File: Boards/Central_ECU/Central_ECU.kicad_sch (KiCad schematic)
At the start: 18 parts, among them U1 STM32G0B1RCTx

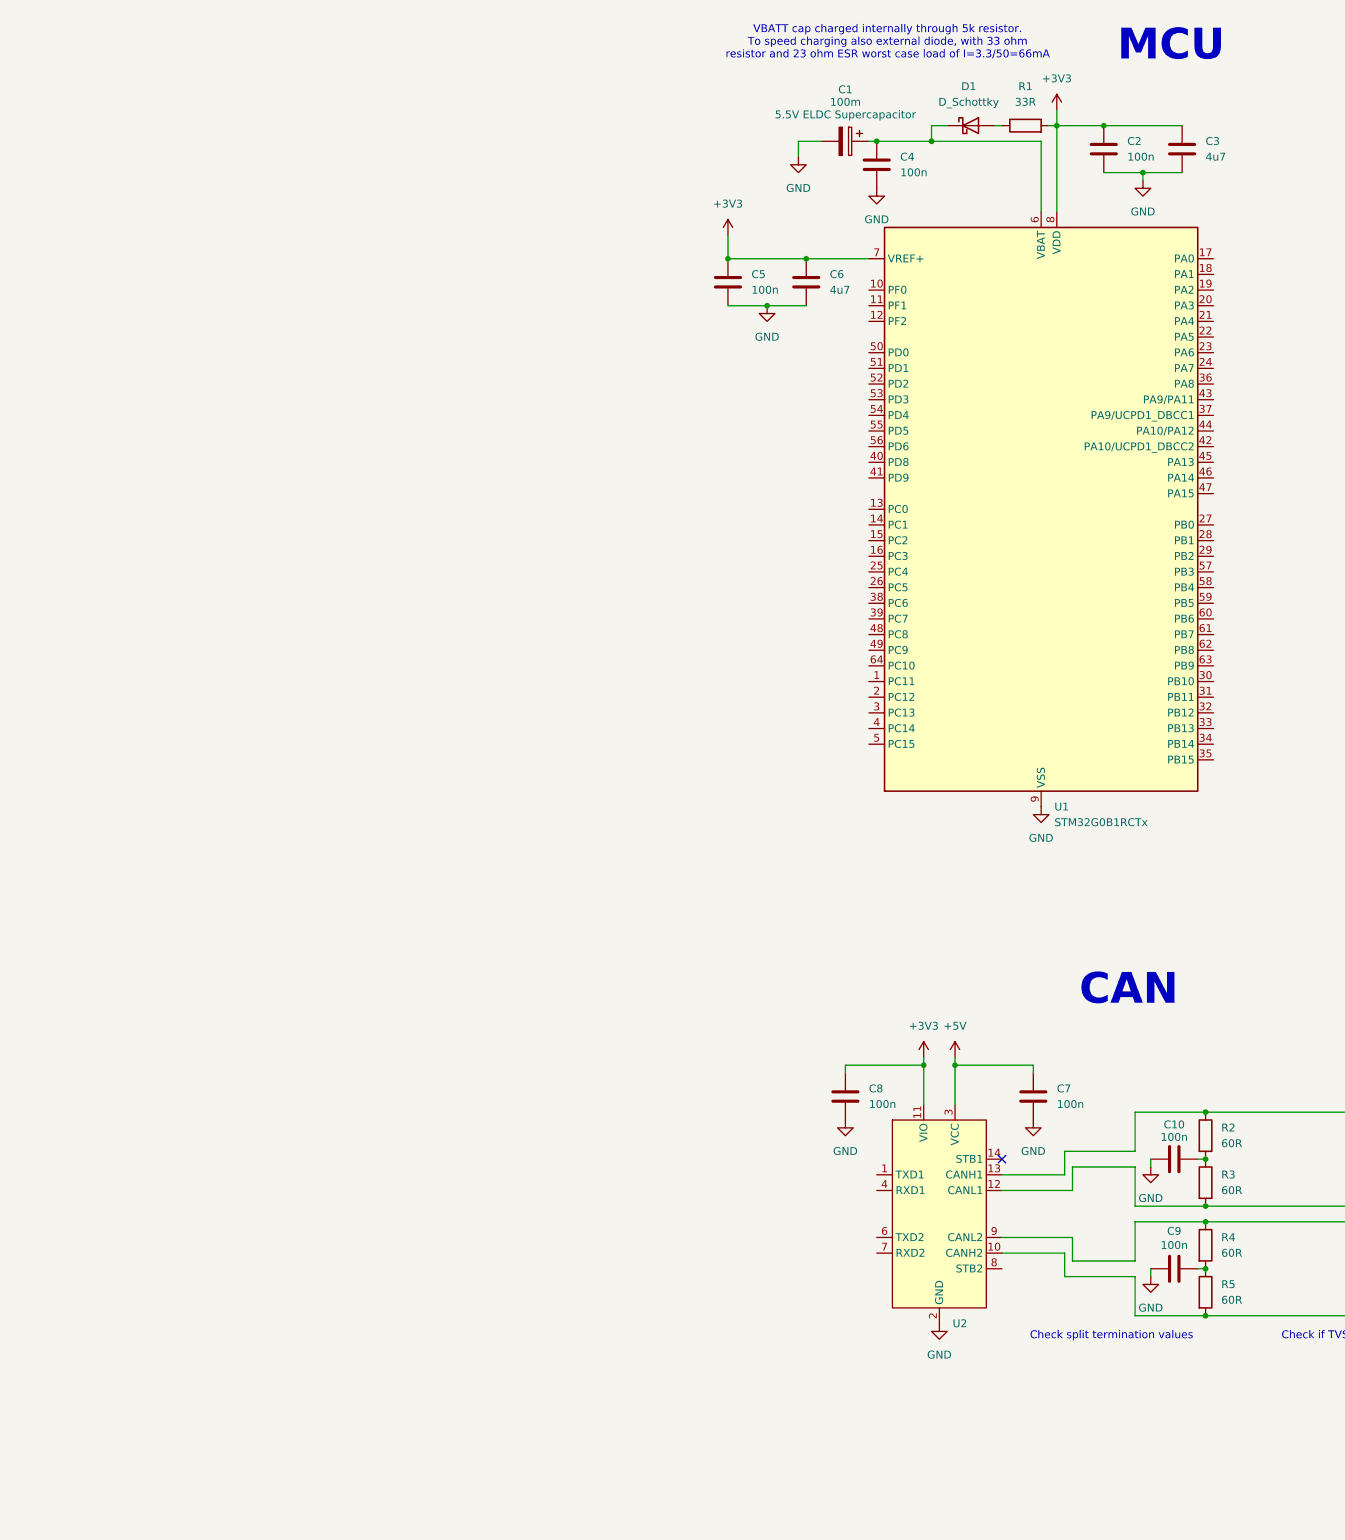
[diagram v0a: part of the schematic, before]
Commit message: Added 422 and crystal
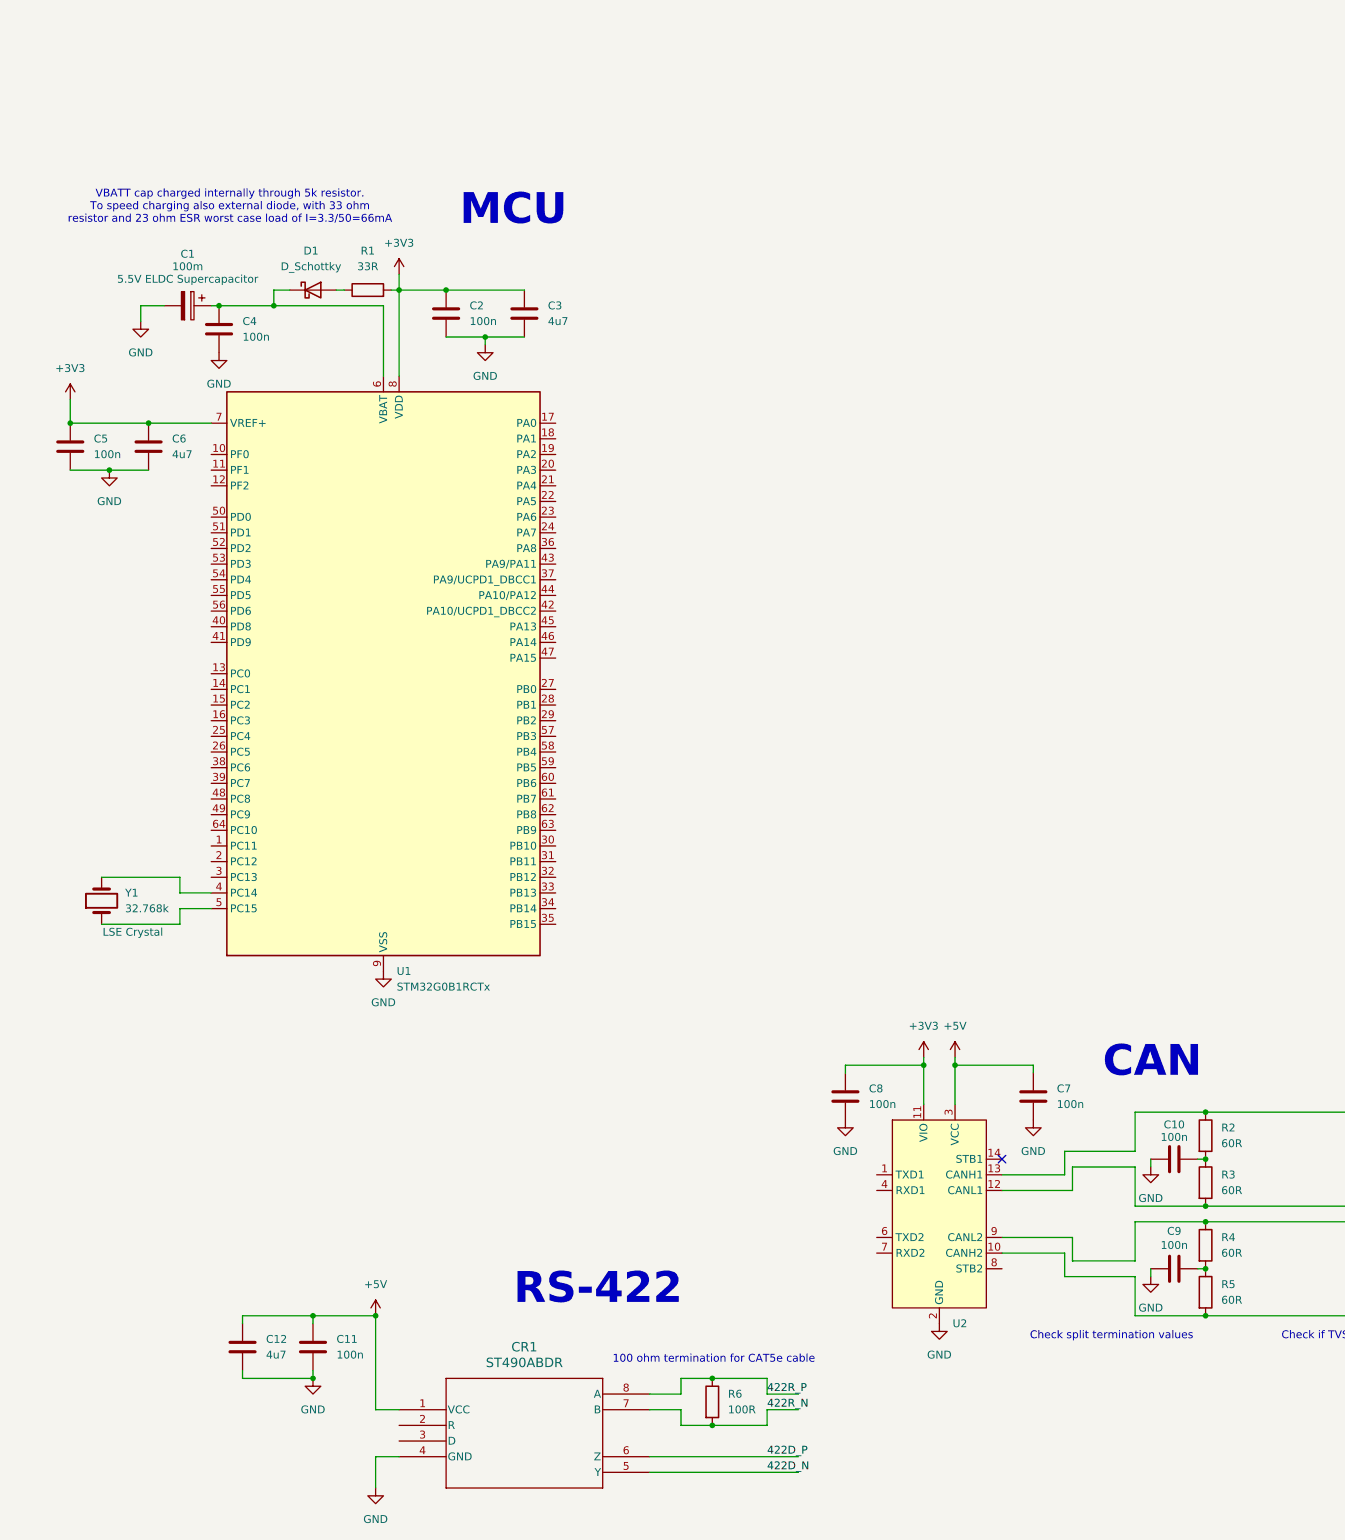
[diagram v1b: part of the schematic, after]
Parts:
- added C11: 100n, symbol Device:C
- added C12: 4u7, symbol Device:C
- added CR1: ST490ABDR, Package_SO:SO-8_3.9x4.9mm_P1.27mm, symbol TS_Symbols:ST490ABDR
- added R6: 100R, symbol Device:R
- added Y1: 32.768k, Crystal:Crystal_SMD_2012-2Pin_2.0x1.2mm, symbol Device:Crystal
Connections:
- net +5V: now also C11.1, C12.1, CR1.1 (VCC)
- net GND: now also C11.2, C12.2, CR1.4 (GND)
- net at U1.4 (PC14): now also Y1.2
- net at U1.5 (PC15): now also Y1.1
- new net 422D_N: CR1.5 (Y)
- new net 422D_P: CR1.6 (Z)
- new net 422R_N: CR1.7 (B), R6.2
- new net 422R_P: CR1.8 (A), R6.1
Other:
- note added: "100 ohm termination for CAT5e cable"
- note added: "RS-422"
- moved on the sheet: C1, C2, C3, C4, C5, C6, D1, R1, U1

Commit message: More to the central mcu plus started on ignitors and valve control
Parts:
- added C13, C14: 12p, symbol Device:C
- added C15, C16: C, symbol Device:C
- added Y2: 8MHz, symbol Device:Crystal
- U1: MPN (none) -> STM32G0B1RCT6
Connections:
- net GND: now also C13.2, C14.2, C15.2, C16.2
- net USART1_RX: now reaches CR1.2 (R)
- net USART1_RX: now also U1.61 (PB7)
- net USART1_TX: now reaches CR1.3 (D)
- net USART1_TX: now also U1.60 (PB6)
- net CAN2_RX: now reaches U2.1 (TXD1)
- net CAN2_RX: now also U1.27 (PB0)
- net CAN2_TX: now reaches U2.4 (RXD1)
- net CAN2_TX: now also U1.28 (PB1)
- net CAN1_RX: now reaches U2.6 (TXD2)
- net CAN1_RX: now also U1.25 (PC4)
- net CAN1_TX: now reaches U2.7 (RXD2)
- net CAN1_TX: now also U1.26 (PC5)
- net at U1.10 (PF0): now also C15.1, Y2.1
- net at U1.11 (PF1): now also C16.1, Y2.2
- net I2C3_SCL: now reaches U1.13 (PC0)
- net I2C3_SDA: now reaches U1.14 (PC1)
- net ADC_0: now reaches U1.17 (PA0)
- net ADC_1: now reaches U1.18 (PA1)
- net ADC_2: now reaches U1.19 (PA2)
- net ADC_3: now reaches U1.20 (PA3)
- net ADC_4: now reaches U1.21 (PA4)
- net SPI_SCK: now reaches U1.22 (PA5)
- net SPI_MISO: now reaches U1.23 (PA6)
- net SPI_MOSI: now reaches U1.24 (PA7)
- net at U1.4 (PC14), Y1.2: now also C14.1
- net USB_D-: now reaches U1.43 (PA9/PA11)
- net USB_D+: now reaches U1.44 (PA10/PA12)
- net SWDIO: now reaches U1.45 (PA13)
- net SWCLK: now reaches U1.46 (PA14)
- net at U1.5 (PC15), Y1.1: now also C13.1
- net UART2_TX: now reaches U1.55 (PD5)
- net UART2_RX: now reaches U1.56 (PD6)
- net I2C2_SCL: now reaches U1.57 (PB3)
- net I2C2_SDA: now reaches U1.58 (PB4)
- net I2C1_SCL: now reaches U1.62 (PB8)
- net I2C1_SDA: now reaches U1.63 (PB9)
- no-connect marks 1 -> 3
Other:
- added sheet Interlocked (ign+nc_valve.kicad_sch)
- moved on the sheet: C1, C10, C11, C12, C2, C3, C4, C5, C6, C7, C8, C9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

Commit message: Some more minor tweaks
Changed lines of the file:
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@@
 	)
 	(sheet
-		(at 437.515 117.475)
+		(at 313.055 194.945)
 		(size 85.09 51.435)
 		(exclude_from_sim no)
@@
 		)
 		(property "Sheetname" "Interlocked"
-			(at 437.515 116.7634 0)
+			(at 313.055 194.2334 0)
 			(effects
 				(font
@@
 		)
 		(property "Sheetfile" "ign+nc_valve.kicad_sch"
-			(at 437.515 169.4946 0)
+			(at 313.055 246.9646 0)
 			(effects
 				(font

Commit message: Added most connectors and hooking up
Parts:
- added J11: Micro_SD_Card, symbol Connector:Micro_SD_Card
- added R19, R20: 27R, symbol Device:R
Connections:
- net USB_D+: now also R20.2; no longer U1.44 (PA10/PA12)
- net USB_D-: now also R19.2; no longer U1.43 (PA9/PA11)
- net CANL2: now reaches R5.2, U2.10 (CANH2)
- net CANL1: now reaches R3.2, U2.12 (CANL1)
- net CANH1: now reaches R2.1, U2.13 (CANH1)
- net CANH2: now reaches R4.1, U2.9 (CANL2)
- net OX_LOW_SENSE: now reaches U1.1 (PC11)
- net EMATCH_1_CONT: now reaches U1.2 (PC12)
- net EMATCH_2_CONT: now reaches U1.3 (PC13)
- net CAN1_AUX: now reaches U1.32 (PB12)
- net CAN2_AUX: now reaches U1.33 (PB13)
- net PGOOD_HS: now reaches U1.34 (PB14)
- net IMON_HS: now reaches U1.35 (PB15)
- net ARM_HS: now reaches U1.38 (PC6)
- net EMATCH_1_FIRE: now reaches U1.39 (PC7)
- net EMATCH_2_FIRE: now reaches U1.48 (PC8)
- net OX_FIRE: now reaches U1.49 (PC9)
- net 12V_SENSE: now reaches U1.64 (PC10)
- net ADC_0 renamed ADC_0 (4S)
- net ADC_1 renamed ADC_1 (2S)
- new net: R19.1, U1.43 (PA9/PA11)
- new net: R20.1, U1.44 (PA10/PA12)
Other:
- added sheet Connectors (connectors.kicad_sch)
- sheet Interlocked ports: added 12V_SENSE, 4S_ARMED_V+, ARM_HS, EMATCH_1+, EMATCH_1-, EMATCH_1_CONT, EMATCH_1_FIRE, EMATCH_2+, EMATCH_2-, EMATCH_2_CONT, EMATCH_2_FIRE, IMON_HS, OX_FIRE, OX_LOW_SENSE, OX_SOLENOID_+, OX_SOLENOID_-, PGOOD_HS, VDDIO; removed none
- note added: "Micro SD"
- moved on the sheet: C1, C10, C11, C12, C13, C14, C15, C16, C2, C3, C4, C5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

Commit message: Nearing completion
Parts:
- added C38, C40: 10u, symbol Device:C
- added C39, C41: 100n, symbol Device:C
- added R35, R36, R37, R38: 20K, symbol Device:R
- added U8: SSD1306, Custom:SSD1306-0.91-OLED-4pin-128x32, symbol TS_Symbols:SSD1306_128x32
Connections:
- net +3V3: now also J11.4 (VDD), C38.1, C39.1, C40.1, C41.1, R35.1, R36.1, R37.1, R38.1, U8.2 (3V3)
- net GND: now also J11.6 (VSS), J11.9 (SHIELD), C38.2, C39.2, C40.2, C41.2, U8.1 (GND)
- net I2C3_SCL: now also U8.3 (SCL)
- net I2C3_SDA: now also U8.4 (SDA)
- net SPI_MISO: now also J11.7 (DAT0), R36.2
- net SPI_MOSI: now also J11.3 (CMD), R37.2
- net SPI_SCK: now also J11.5 (CLK), R35.2
- net SPI_SD_CS: now reaches U1.36 (PA8)
- net SPI_SD_CS: now also J11.2 (DAT3/CD), R38.2
- no-connect marks 3 -> 15
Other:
- sheet Connectors ports: added I2CA_SCL, I2CA_SDA, I2CB_SCL, I2CB_SDA, UART_RX, UART_TX; removed none
- note added: "Display"
- note added: "TODO: Add some LED's - Both power supplies - GPIO controlled Add a buzzer? Break out generic pins"
- moved on the sheet: C5, C6

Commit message: For review
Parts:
- added D2, D3, D4: LED, LED_SMD:LED_1206_3216Metric, symbol Device:LED
- added H1, H2, H3, H4: ~, MountingHole:MountingHole_3.2mm_M3_DIN965_Pad_TopOnly, symbol Mechanical:MountingHole_Pad
- added R13: 330R, Resistor_SMD:R_0805_2012Metric, symbol Device:R
- added R14: 220R, Resistor_SMD:R_0805_2012Metric, symbol Device:R
- added R15: 1K, Resistor_SMD:R_0805_2012Metric, symbol Device:R
- added R16, R17, R18, R19: 10K, Resistor_SMD:R_0805_2012Metric, symbol Device:R
- added TP1: RTC_CAP, TestPoint:TestPoint_Keystone_5005-5009_Compact, symbol Connector:TestPoint_Small
- added TP10: CANTX2, TestPoint:TestPoint_Keystone_5005-5009_Compact, symbol Connector:TestPoint_Small
- added TP11: CANRX2, TestPoint:TestPoint_Keystone_5005-5009_Compact, symbol Connector:TestPoint_Small
- added TP12: ARMSIG, TestPoint:TestPoint_Keystone_5005-5009_Compact, symbol Connector:TestPoint_Small
- added TP13: EMCH1, TestPoint:TestPoint_Keystone_5005-5009_Compact, symbol Connector:TestPoint_Small
- added TP14: RS422TX, TestPoint:TestPoint_Keystone_5005-5009_Compact, symbol Connector:TestPoint_Small
- added TP15: EMCH2, TestPoint:TestPoint_Keystone_5005-5009_Compact, symbol Connector:TestPoint_Small
- added TP16: RS422RX, TestPoint:TestPoint_Keystone_5005-5009_Compact, symbol Connector:TestPoint_Small
- added TP17: OXFIRE, TestPoint:TestPoint_Keystone_5005-5009_Compact, symbol Connector:TestPoint_Small
- added TP18: SENSE12, TestPoint:TestPoint_Keystone_5005-5009_Compact, symbol Connector:TestPoint_Small
- added TP19: SENSEOX, TestPoint:TestPoint_Keystone_5005-5009_Compact, symbol Connector:TestPoint_Small
- added TP2: ADC4S, TestPoint:TestPoint_Keystone_5005-5009_Compact, symbol Connector:TestPoint_Small
- added TP20: CONT1, TestPoint:TestPoint_Keystone_5005-5009_Compact, symbol Connector:TestPoint_Small
- added TP21: CONT2, TestPoint:TestPoint_Keystone_5005-5009_Compact, symbol Connector:TestPoint_Small
- added TP22: IMON, TestPoint:TestPoint_Keystone_5005-5009_Compact, symbol Connector:TestPoint_Small
- added TP23: PGOOD, TestPoint:TestPoint_Keystone_5005-5009_Compact, symbol Connector:TestPoint_Small
- added TP24: 7.4V, TestPoint:TestPoint_Keystone_5005-5009_Compact, symbol Connector:TestPoint
- added TP25: 5V, TestPoint:TestPoint_Keystone_5005-5009_Compact, symbol Connector:TestPoint
- added TP26: 3.3V, TestPoint:TestPoint_Keystone_5005-5009_Compact, symbol Connector:TestPoint
- added TP27, TP28: GND, TestPoint:TestPoint_Bridge_Pitch2.54mm_Drill1.3mm, symbol Connector:TestPoint
- added TP3: ADC2S, TestPoint:TestPoint_Keystone_5005-5009_Compact, symbol Connector:TestPoint_Small
- added TP31: ADC2, TestPoint:TestPoint_Keystone_5005-5009_Compact, symbol Connector:TestPoint_Small
- added TP32: ADC3, TestPoint:TestPoint_Keystone_5005-5009_Compact, symbol Connector:TestPoint_Small
- added TP33: ADC4, TestPoint:TestPoint_Keystone_5005-5009_Compact, symbol Connector:TestPoint_Small
- added TP4: SPISCK, TestPoint:TestPoint_Keystone_5005-5009_Compact, symbol Connector:TestPoint_Small
- added TP5: SPIMISO, TestPoint:TestPoint_Keystone_5005-5009_Compact, symbol Connector:TestPoint_Small
- added TP6: SPIMOSI, TestPoint:TestPoint_Keystone_5005-5009_Compact, symbol Connector:TestPoint_Small
- added TP7: SPICS, TestPoint:TestPoint_Keystone_5005-5009_Compact, symbol Connector:TestPoint_Small
- added TP8: CANTX1, TestPoint:TestPoint_Keystone_5005-5009_Compact, symbol Connector:TestPoint_Small
- added TP9: CANRX1, TestPoint:TestPoint_Keystone_5005-5009_Compact, symbol Connector:TestPoint_Small
- C1: renamed from C38; footprint (none) -> Capacitor_SMD:C_0805_2012Metric
- C10: renamed from C6; footprint (none) -> Capacitor_SMD:C_0805_2012Metric
- C11: renamed from C15; value C -> ?; footprint (none) -> Capacitor_SMD:C_0402_1005Metric
- C12: renamed from C16; value C -> ?; footprint (none) -> Capacitor_SMD:C_0402_1005Metric
- C13: renamed from C7; footprint (none) -> Capacitor_SMD:C_0805_2012Metric
- C14: renamed from C8; footprint (none) -> Capacitor_SMD:C_0805_2012Metric
- C15: renamed from C10; footprint (none) -> Capacitor_SMD:C_0805_2012Metric
- C16: renamed from C12; footprint (none) -> Capacitor_SMD:C_0805_2012Metric
- C17: renamed from C11; footprint (none) -> Capacitor_SMD:C_0805_2012Metric
- C18: renamed from C9; footprint (none) -> Capacitor_SMD:C_0805_2012Metric
- C19: renamed from C14; footprint (none) -> Capacitor_SMD:C_0402_1005Metric
- C2: renamed from C39; footprint (none) -> Capacitor_SMD:C_0805_2012Metric
- C20: renamed from C13; footprint (none) -> Capacitor_SMD:C_0402_1005Metric
- C3: renamed from C41; footprint (none) -> Capacitor_SMD:C_0805_2012Metric
- C4: renamed from C40; footprint (none) -> Capacitor_SMD:C_0805_2012Metric
- C5: renamed from C1; footprint (none) -> Capacitor_THT:CP_Radial_D14.0mm_P5.00mm; MPN (none) -> RSCBN1045R5G07014T
- C6: renamed from C2; footprint (none) -> Capacitor_SMD:C_0805_2012Metric
- C7: renamed from C3; footprint (none) -> Capacitor_SMD:C_0805_2012Metric
- C8: renamed from C4; footprint (none) -> Capacitor_SMD:C_0805_2012Metric
- C9: renamed from C5; footprint (none) -> Capacitor_SMD:C_0805_2012Metric
- CR1: MPN (none) -> ST490ABDR
- D1: footprint (none) -> Diode_SMD:D_SOD-882; MPN (none) -> CTS05S40,L3F
- J1: renamed from J11; footprint (none) -> Connector_Card:microSD_HC_Molex_47219-2001; MPN (none) -> 0472192001
- R1: footprint (none) -> Resistor_SMD:R_0805_2012Metric
- R10: renamed from R4; footprint (none) -> Resistor_SMD:R_0805_2012Metric
- R11: renamed from R6; footprint (none) -> Resistor_SMD:R_0805_2012Metric
- R12: renamed from R5; footprint (none) -> Resistor_SMD:R_0805_2012Metric
- R2: renamed from R35; footprint (none) -> Resistor_SMD:R_0805_2012Metric
- R3: renamed from R36; footprint (none) -> Resistor_SMD:R_0805_2012Metric
- R4: renamed from R37; footprint (none) -> Resistor_SMD:R_0805_2012Metric
- R5: renamed from R38; footprint (none) -> Resistor_SMD:R_0805_2012Metric
- R6: renamed from R19; footprint (none) -> Resistor_SMD:R_0805_2012Metric
- R7: renamed from R20; footprint (none) -> Resistor_SMD:R_0805_2012Metric
- R8: renamed from R2; footprint (none) -> Resistor_SMD:R_0805_2012Metric
- R9: renamed from R3; footprint (none) -> Resistor_SMD:R_0805_2012Metric
- U1: renamed from U8; MPN (none) -> N/A; now left out of the parts list
- U3: renamed from U2; value ~ -> TCAN1046; MPN (none) -> TCAN1046AVDYYRQ1
- Y1: renamed from Y2; footprint (none) -> Crystal:Crystal_SMD_Abracon_ABM3B-4Pin_5.0x3.2mm
- renumbered U1 to U2, Y1 to Y2
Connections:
- net +3V3: now also R16.2, R17.2, R18.2, R19.2, TP26.1
- net +5V: now also TP25.1
- net +7V4: now also R13.1, TP24.1
- net 12V_SENSE: now also TP18.1
- net ADC_0 (4S): now also TP2.1
- net ADC_1 (2S): now also TP3.1
- net ADC_2: now also TP31.1
- net ADC_3: now also TP32.1
- net ADC_4: now also TP33.1
- net ARM_HS: now also TP12.1
- net CAN1_RX: now also U2.27 (PB0), U3.1 (TXD1), TP8.1; no longer U2.25 (PC4), U3.6 (TXD2)
- net CAN1_TX: now also U2.28 (PB1), U3.4 (RXD1), TP9.1; no longer U2.26 (PC5), U3.7 (RXD2)
- net CAN2_RX: now also U2.25 (PC4), U3.6 (TXD2), TP10.1; no longer U2.27 (PB0), U3.1 (TXD1)
- net CAN2_TX: now also U2.26 (PC5), U3.7 (RXD2), TP11.1; no longer U2.28 (PB1), U3.4 (RXD1)
- net EMATCH_1_CONT: now also TP20.1
- net EMATCH_1_FIRE: now also TP13.1
- net EMATCH_2_CONT: now also TP21.1
- net EMATCH_2_FIRE: now also TP15.1
- net GND: now also D2.1 (K), D3.1 (K), D4.1 (K), H1.1, H2.1, H3.1, H4.1, TP27.1, TP28.1
- net I2C1_SCL: now also R17.1
- net I2C1_SDA: now also R16.1
- net I2C2_SCL: now also R19.1
- net I2C2_SDA: now also R18.1
- net IMON_HS: now also TP22.1
- net OX_FIRE: now also TP17.1
- net OX_LOW_SENSE: now also TP19.1
- net PGOOD_HS: now also TP23.1
- net SPI_MISO: now also TP5.1
- net SPI_MOSI: now also TP6.1
- net SPI_SCK: now also TP4.1
- net SPI_SD_CS: now also TP7.1
- net USART1_RX: now also TP16.1
- net USART1_TX: now also TP14.1
- net at C5.1, C8.1, D1.1 (K)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: now also TP1.1
- net LED1: now reaches U2.50 (PD0)
- net LED1: now also R14.1
- net E1: now reaches U2.51 (PD1)
- net E2: now reaches U2.52 (PD2)
- net E3: now reaches U2.53 (PD3)
- net E4: now reaches U2.54 (PD4)
- new net: D3.2 (A), R14.2
- new net: D4.2 (A), R15.2
- new net: D2.2 (A), R13.2
- new net 4S_V+: R15.1
- no-connect marks 15 -> 16
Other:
- sheet Connectors ports: added E1, E2, E3, E4; removed none
- note added: "Connectors"
- note added: "Spicy Stuff"
- note removed: "TODO: Add some LED's - Both power supplies - GPIO controlled Add a buzzer? Break out generic pins"
- moved on the sheet: C13, C14, C15, C18, C8, R10, R12, R8, R9, U3
